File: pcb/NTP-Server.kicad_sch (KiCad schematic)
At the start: 19 parts, among them J1 Button1, J2 Button2, J3 USB_C, J4 Raspberry_Pi_2_3, J5 VCC-Monitor, J6 I2C, U1 GT-U7, U2 DS3231MZ

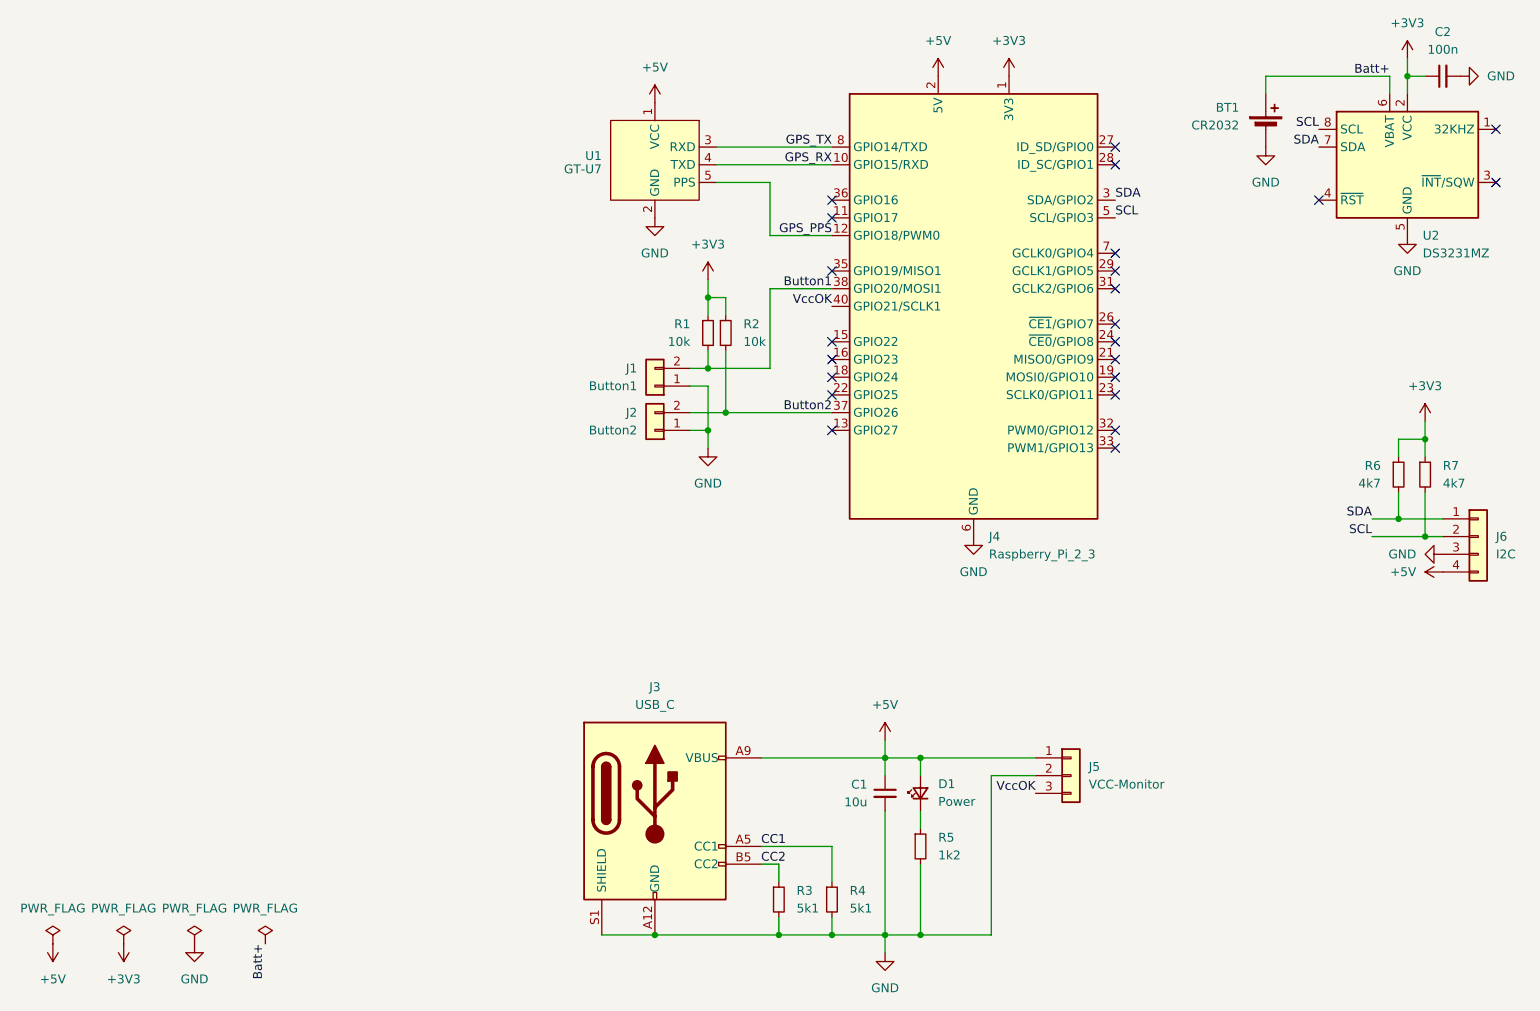
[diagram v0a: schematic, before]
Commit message: feat!: complete redesign
Remove unneeded parts and make the whole board a lot smaller
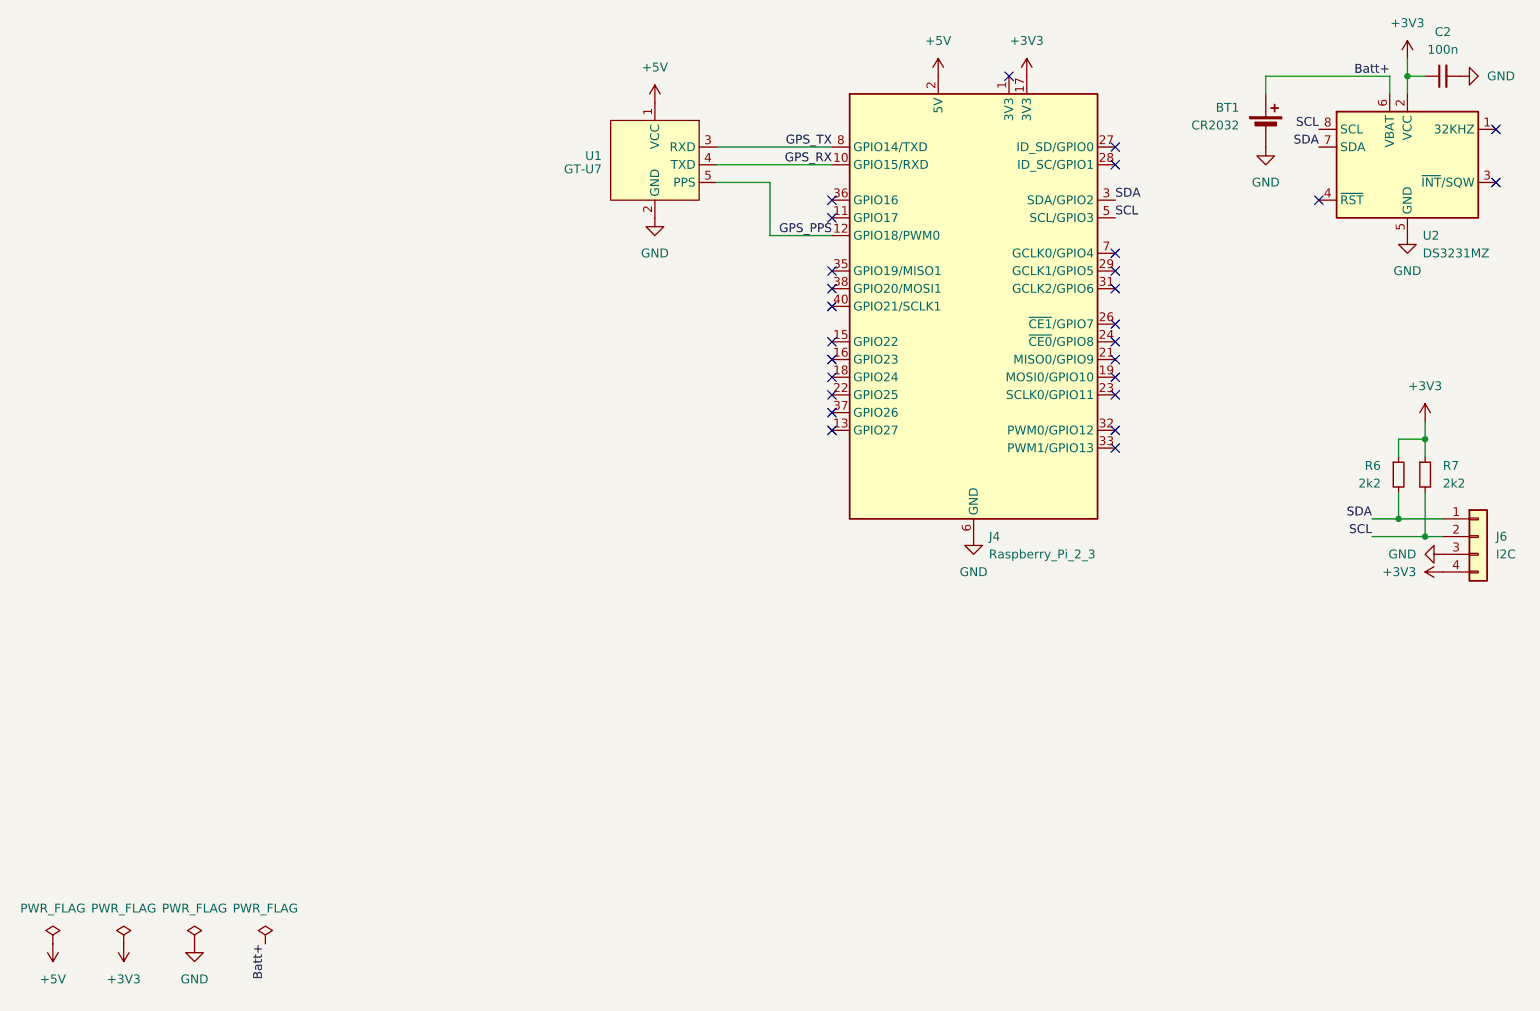
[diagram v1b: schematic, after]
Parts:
- removed C1: 10u, Capacitor_SMD:C_1206_3216Metric_Pad1.33x1.80mm_HandSolder, symbol Device:C_Small
- removed D1: Power, LED_SMD:LED_0603_1608Metric_Pad1.05x0.95mm_HandSolder, symbol Device:LED_Small
- removed J1: Button1, Connector_JST:JST_PH_B2B-PH-K_1x02_P2.00mm_Vertical, symbol Connector_Generic:Conn_01x02
- removed J2: Button2, Connector_JST:JST_PH_B2B-PH-K_1x02_P2.00mm_Vertical, symbol Connector_Generic:Conn_01x02
- removed J3: USB_C, Connector_USB:USB_C_Receptacle_GCT_USB4125-xx-x_6P_TopMnt_Horizontal, symbol Connector:USB_C_Receptacle_PowerOnly_6P
- removed J5: VCC-Monitor, Connector_PinHeader_2.54mm:PinHeader_1x03_P2.54mm_Vertical, symbol Connector_Generic:Conn_01x03
- removed R1, R2: 10k, Resistor_SMD:R_0603_1608Metric_Pad0.98x0.95mm_HandSolder, symbol Device:R_Small
- removed R3, R4: 5k1, Resistor_SMD:R_0603_1608Metric_Pad0.98x0.95mm_HandSolder, symbol Device:R_Small
- removed R5: 1k2, Resistor_SMD:R_0603_1608Metric_Pad0.98x0.95mm_HandSolder, symbol Device:R_Small
- BT1: footprint Battery:BatteryHolder_Keystone_1060_1x2032 -> Connector_Molex:Molex_PicoBlade_53047-0210_1x02_P1.25mm_Vertical
- J4: footprint My_Footprints:RPi_HAT_FullSize -> Connector_PinSocket_2.54mm:PinSocket_2x20_P2.54mm_Vertical
- R6, R7: value 4k7 -> 2k2
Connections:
- net +3V3: now also J6.4 (Pin_4); no longer J4.1 (3V3)
- net +5V: no longer J6.4 (Pin_4)
- net Button1: no longer names the net of J4.38 (GPIO20/MOSI1)
- net Button2: no longer names the net of J4.37 (GPIO26)
- net VccOK: no longer names the net of J4.40 (GPIO21/SCLK1)
- no-connect marks 23 -> 27
